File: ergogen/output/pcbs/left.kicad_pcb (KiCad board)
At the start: 2 copper layers, 118.4 x 104.8 mm, 29 parts

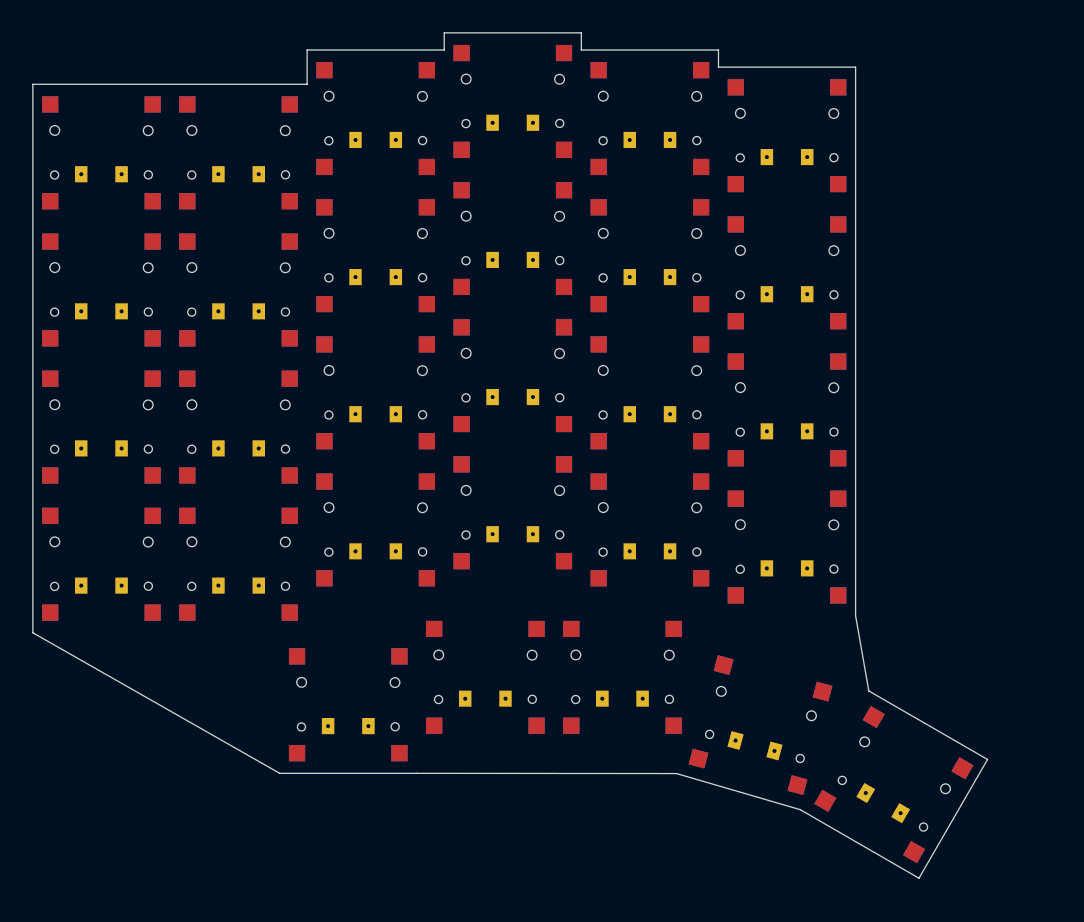
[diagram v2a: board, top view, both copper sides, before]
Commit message: feat: improved outlines
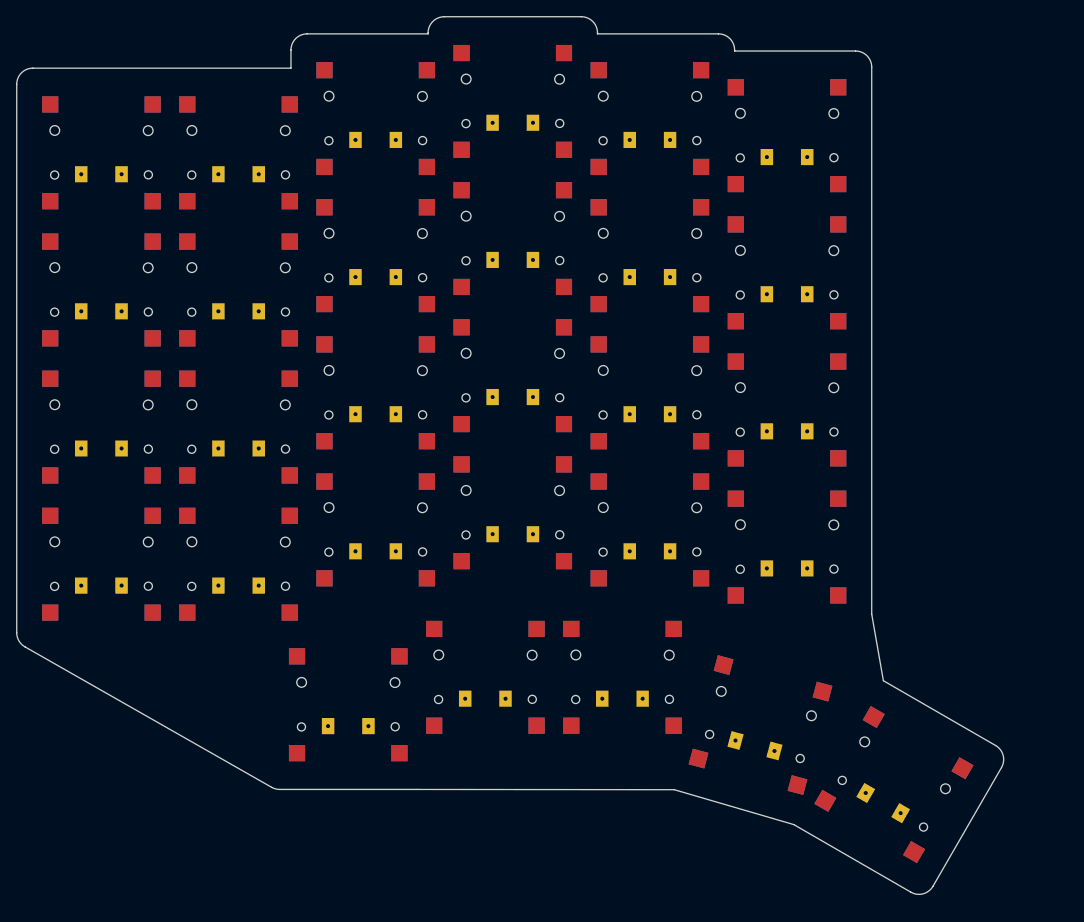
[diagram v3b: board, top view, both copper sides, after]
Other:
- board size 118.4 x 104.8 mm -> 122.4 x 108.8 mm
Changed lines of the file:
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@@
 (model "models/PG1316S--装配体.STEP" (offset (xyz -4.75 -6.25 -10.25)) (scale (xyz 1 1 1)) (rotate (xyz 0 0 0)))
 )
-  (gr_line (start 91.5 108.5) (end 91.5 40.5) (layer Edge.Cuts) (stroke (width 0.15) (type default)))
-(gr_line (start 91.5 40.5) (end 125.5 40.5) (layer Edge.Cuts) (stroke (width 0.15) (type default)))
-(gr_line (start 125.5 40.5) (end 125.5 36.25) (layer Edge.Cuts) (stroke (width 0.15) (type default)))
-(gr_line (start 125.5 36.25) (end 142.5 36.25) (layer Edge.Cuts) (stroke (width 0.15) (type default)))
-(gr_line (start 142.5 36.25) (end 142.5 34.125) (layer Edge.Cuts) (stroke (width 0.15) (type default)))
-(gr_line (start 142.5 34.125) (end 159.5 34.125) (layer Edge.Cuts) (stroke (width 0.15) (type default)))
-(gr_line (start 159.5 34.125) (end 159.5 36.25) (layer Edge.Cuts) (stroke (width 0.15) (type default)))
-(gr_line (start 159.5 36.25) (end 176.5 36.25) (layer Edge.Cuts) (stroke (width 0.15) (type default)))
-(gr_line (start 176.5 36.25) (end 176.5 38.375) (layer Edge.Cuts) (stroke (width 0.15) (type default)))
-(gr_line (start 176.5 38.375) (end 193.5 38.375) (layer Edge.Cuts) (stroke (width 0.15) (type default)))
-(gr_line (start 193.5 38.375) (end 193.5 106.375) (layer Edge.Cuts) (stroke (width 0.15) (type default)))
-(gr_line (start 193.5 106.375) (end 195.1372799 115.70819429999999) (layer Edge.Cuts) (stroke (width 0.15) (type default)))
-(gr_line (start 195.1372799 115.70819429999999) (end 209.8597117 124.20819429999999) (layer Edge.Cuts) (stroke (width 0.15) (type default)))
-(gr_line (start 209.8597117 124.20819429999999) (end 201.3597117 138.93062609999998) (layer Edge.Cuts) (stroke (width 0.15) (type default)))
-(gr_line (start 201.3597117 138.93062609999998) (end 186.6372799 130.43062609999998) (layer Edge.Cuts) (stroke (width 0.15) (type default)))
-(gr_line (start 186.6372799 130.43062609999998) (end 171.3055208 125.9554228) (layer Edge.Cuts) (stroke (width 0.15) (type default)))
-(gr_line (start 171.3055208 125.9554228) (end 139.1 125.925) (layer Edge.Cuts) (stroke (width 0.15) (type default)))
-(gr_line (start 139.1 125.925) (end 122.1 125.925) (layer Edge.Cuts) (stroke (width 0.15) (type default)))
-(gr_line (start 122.1 125.925) (end 91.5 108.5) (layer Edge.Cuts) (stroke (width 0.15) (type default)))
+  (gr_line (start 89.5 108.5) (end 89.5 40.5) (layer Edge.Cuts) (stroke (width 0.15) (type default)))
+(gr_arc (start 91.5 38.5) (mid 90.0857864 39.0857864) (end 89.5 40.5) (layer Edge.Cuts) (stroke (width 0.15) (type default)))
+(gr_line (start 91.5 38.5) (end 123.5 38.5) (layer Edge.Cuts) (stroke (width 0.15) (type default)))
+(gr_line (start 123.5 38.5) (end 123.5 36.25) (layer Edge.Cuts) (stroke (width 0.15) (type default)))
+(gr_arc (start 125.5 34.25) (mid 124.0857864 34.8357864) (end 123.5 36.25) (layer Edge.Cuts) (stroke (width 0.15) (type default)))
+(gr_line (start 125.5 34.25) (end 140.5 34.25) (layer Edge.Cuts) (stroke (width 0.15) (type default)))
+(gr_line (start 140.5 34.25) (end 140.5 34.125) (layer Edge.Cuts) (stroke (width 0.15) (type default)))
+(gr_arc (start 142.5 32.125) (mid 141.0857864 32.7107864) (end 140.5 34.125) (layer Edge.Cuts) (stroke (width 0.15) (type default)))
+(gr_line (start 142.5 32.125) (end 159.5 32.125) (layer Edge.Cuts) (stroke (width 0.15) (type default)))
+(gr_arc (start 161.5 34.125) (mid 160.9142136 32.7107864) (end 159.5 32.125) (layer Edge.Cuts) (stroke (width 0.15) (type default)))
+(gr_line (start 161.5 34.125) (end 161.5 34.25) (layer Edge.Cuts) (stroke (width 0.15) (type default)))
+(gr_line (start 161.5 34.25) (end 176.5 34.25) (layer Edge.Cuts) (stroke (width 0.15) (type default)))
+(gr_arc (start 178.5 36.25) (mid 177.9142136 34.8357864) (end 176.5 34.25) (layer Edge.Cuts) (stroke (width 0.15) (type default)))
+(gr_line (start 178.5 36.25) (end 178.5 36.375) (layer Edge.Cuts) (stroke (width 0.15) (type default)))
+(gr_line (start 178.5 36.375) (end 193.5 36.375) (layer Edge.Cuts) (stroke (width 0.15) (type default)))
+(gr_arc (start 195.5 38.375) (mid 194.9142136 36.9607864) (end 193.5 36.375) (layer Edge.Cuts) (stroke (width 0.15) (type default)))
+(gr_line (start 195.5 38.375) (end 195.5 106.20090349023451) (layer Edge.Cuts) (stroke (width 0.15) (type default)))
+(gr_line (start 195.5 106.20090349023451) (end 196.94587069424657 114.44298361476274) (layer Edge.Cuts) (stroke (width 0.15) (type default)))
+(gr_line (start 196.94587069424657 114.44298361476254) (end 210.85971170000002 122.47614349999999) (layer Edge.Cuts) (stroke (width 0.15) (type default)))
+(gr_arc (start 211.59176250000002 125.20819429999999) (mid 211.7915633 123.69055619999999) (end 210.85971170000002 122.47614349999999) (layer Edge.Cuts) (stroke (width 0.15) (type default)))
+(gr_line (start 211.5917625 125.20819429999999) (end 203.0917625 139.93062609999998) (layer Edge.Cuts) (stroke (width 0.15) (type default)))
+(gr_arc (start 200.3597117 140.66267689999998) (mid 201.8773498 140.86247769999997) (end 203.0917625 139.93062609999998) (layer Edge.Cuts) (stroke (width 0.15) (type default)))
+(gr_line (start 200.3597117 140.66267689999998) (end 185.84577629334714 132.28305234935004) (layer Edge.Cuts) (stroke (width 0.15) (type default)))
+(gr_line (start 185.84577629334714 132.28305234935004) (end 171.0186700831264 127.95515271248252) (layer Edge.Cuts) (stroke (width 0.15) (type default)))
+(gr_line (start 171.0186700831264 127.9551527124825) (end 139.1 127.925) (layer Edge.Cuts) (stroke (width 0.15) (type default)))
+(gr_line (start 139.0981107 127.9249991) (end 122.1 127.925) (layer Edge.Cuts) (stroke (width 0.15) (type default)))
+(gr_arc (start 121.11032279999999 127.6629698) (mid 121.58811109999999 127.858383) (end 122.1 127.925) (layer Edge.Cuts) (stroke (width 0.15) (type default)))
+(gr_line (start 121.11032279999999 127.6629698) (end 90.5103228 110.2379698) (layer Edge.Cuts) (stroke (width 0.15) (type default)))
+(gr_arc (start 89.5 108.5) (mid 89.7709317 109.5051481) (end 90.5103228 110.2379698) (layer Edge.Cuts) (stroke (width 0.15) (type default)))
 )

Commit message: feat: refining bottom row
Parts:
- removed S29: , CPG1316S01D02_reversible
- moved S28 24.9 mm to (206.1, 114.7)
- moved S25 20.5 mm to (151.0, 115.7)
- moved S26 20.5 mm to (168.0, 115.7)
- moved S27 20.5 mm to (185.0, 115.7)
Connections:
- S25 pad 1: C1 -> C2
- S26 pad 1: C2 -> C3
- S26 pad 2: mid_home -> outward_home
- S27 pad 1: C3 -> C4
- S27 pad 2: outward_home -> small_thumbkey_home
- S28 pad 1: C4 -> C5
- S28 pad 2: small_thumbkey_home -> thumbkey_home
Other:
- board size 122.4 x 108.8 mm -> 129 x 95 mm

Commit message: feat: thumb key 1.5u (thanks @chadtrans)
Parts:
- turned S28 to 75 degrees
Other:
- board size 129 x 95 mm -> 130 x 99.4 mm
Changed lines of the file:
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@@
 )
 (footprint "CPG1316S01D02_reversible"
-(at 206.1051848 114.6999809 -15)
+(at 206.1051848 114.6999809 75)
 (layer F.Cu)
 (attr smd)
-(property "Reference" "S28" hide (at 0 0 -15) (layer "F.SilkS") (effects (font (size 1 1) (thickness 0.15))))
-(pad "1" thru_hole rect (at -2.5 2.65 -15) (size 1.55 2) (drill 0.5) (layers "*.Cu" "*.Mask") (remove_unused_layers no) (thermal_bridge_angle 45) (net 26 "C5"))
-(pad "2" thru_hole rect (at 2.5 2.65 -15) (size 1.55 2) (drill 0.5) (layers "*.Cu" "*.Mask") (remove_unused_layers no) (thermal_bridge_angle 45) (net 34 "thumbkey_home"))
-(pad "3" smd rect (at -6.35 -6 -15) (size 2 2) (layers "F.Cu" "F.Paste" "F.Mask") (thermal_bridge_angle 45) (net 0 ""))
-(pad "3" smd rect (at -6.35 -6 -15) (size 2 2) (layers "B.Cu" "B.Paste" "B.Mask") (thermal_bridge_angle 45) (net 0 ""))
-(pad "3" smd rect (at -6.35 6 -15) (size 2 2) (layers "F.Cu" "F.Paste" "F.Mask") (thermal_bridge_angle 45) (net 0 ""))
-(pad "3" smd rect (at -6.35 6 -15) (size 2 2) (layers "B.Cu" "B.Paste" "B.Mask") (thermal_bridge_angle 45) (net 0 ""))
-(pad "3" smd rect (at 6.35 -6 -15) (size 2 2) (layers "F.Cu" "F.Paste" "F.Mask") (thermal_bridge_angle 45) (net 0 ""))
-(pad "3" smd rect (at 6.35 -6 -15) (size 2 2) (layers "B.Cu" "B.Paste" "B.Mask") (thermal_bridge_angle 45) (net 0 ""))
-(pad "3" smd rect (at 6.35 6 -15) (size 2 2) (layers "F.Cu" "F.Paste" "F.Mask") (thermal_bridge_angle 45) (net 0 ""))
-(pad "3" smd rect (at 6.35 6 -15) (size 2 2) (layers "B.Cu" "B.Paste" "B.Mask") (thermal_bridge_angle 45) (net 0 ""))
+(property "Reference" "S28" hide (at 0 0 75) (layer "F.SilkS") (effects (font (size 1 1) (thickness 0.15))))
+(pad "1" thru_hole rect (at -2.5 2.65 75) (size 1.55 2) (drill 0.5) (layers "*.Cu" "*.Mask") (remove_unused_layers no) (thermal_bridge_angle 45) (net 26 "C5"))
+(pad "2" thru_hole rect (at 2.5 2.65 75) (size 1.55 2) (drill 0.5) (layers "*.Cu" "*.Mask") (remove_unused_layers no) (thermal_bridge_angle 45) (net 34 "thumbkey_home"))
+(pad "3" smd rect (at -6.35 -6 75) (size 2 2) (layers "F.Cu" "F.Paste" "F.Mask") (thermal_bridge_angle 45) (net 0 ""))
+(pad "3" smd rect (at -6.35 -6 75) (size 2 2) (layers "B.Cu" "B.Paste" "B.Mask") (thermal_bridge_angle 45) (net 0 ""))
+(pad "3" smd rect (at -6.35 6 75) (size 2 2) (layers "F.Cu" "F.Paste" "F.Mask") (thermal_bridge_angle 45) (net 0 ""))
+(pad "3" smd rect (at -6.35 6 75) (size 2 2) (layers "B.Cu" "B.Paste" "B.Mask") (thermal_bridge_angle 45) (net 0 ""))
+(pad "3" smd rect (at 6.35 -6 75) (size 2 2) (layers "F.Cu" "F.Paste" "F.Mask") (thermal_bridge_angle 45) (net 0 ""))
+(pad "3" smd rect (at 6.35 -6 75) (size 2 2) (layers "B.Cu" "B.Paste" "B.Mask") (thermal_bridge_angle 45) (net 0 ""))
+(pad "3" smd rect (at 6.35 6 75) (size 2 2) (layers "F.Cu" "F.Paste" "F.Mask") (thermal_bridge_angle 45) (net 0 ""))
+(pad "3" smd rect (at 6.35 6 75) (size 2 2) (layers "B.Cu" "B.Paste" "B.Mask") (thermal_bridge_angle 45) (net 0 ""))
 (fp_circle (center -5.8 2.75) (end -5.3 2.75) (stroke (width 0.1) (type default)) (fill none) (layer "Edge.Cuts"))
 (fp_circle (center -5.781 -2.773) (end -6.381 -2.773) (stroke (width 0.1) (type default)) (fill none) (layer "Edge.Cuts"))
@@
 (gr_line (start 178.5 36.375) (end 193.5 36.375) (layer Edge.Cuts) (stroke (width 0.15) (type default)))
 (gr_arc (start 195.5 38.375) (mid 194.9142136 36.9607864) (end 193.5 36.375) (layer Edge.Cuts) (stroke (width 0.15) (type default)))
-(gr_line (start 195.5 38.375) (end 195.5 103.64496668730112) (layer Edge.Cuts) (stroke (width 0.15) (type default)))
-(gr_line (start 195.5 103.64496668730112) (end 199.4917811 102.3827159) (layer Edge.Cuts) (stroke (width 0.15) (type default)))
-(gr_arc (start 200.6124153 102.3577978) (mid 200.05031680000002 102.2901437) (end 199.4917811 102.3827159) (layer Edge.Cuts) (stroke (width 0.15) (type default)))
-(gr_line (start 200.61241529999998 102.3577978) (end 217.03315429999998 106.7577216) (layer Edge.Cuts) (stroke (width 0.15) (type default)))
-(gr_arc (start 218.4473679 109.20721139999999) (mid 218.24756709999997 107.68957329999999) (end 217.03315429999998 106.7577216) (layer Edge.Cuts) (stroke (width 0.15) (type default)))
-(gr_line (start 218.4473679 109.2072114) (end 214.04744409999998 125.6279504) (layer Edge.Cuts) (stroke (width 0.15) (type default)))
-(gr_arc (start 211.59795429999997 127.042164) (mid 213.11559239999997 126.84236320000001) (end 214.04744409999998 125.6279504) (layer Edge.Cuts) (stroke (width 0.15) (type default)))
-(gr_line (start 211.5979543 127.042164) (end 195.61215207761586 122.7587811595346) (layer Edge.Cuts) (stroke (width 0.15) (type default)))
-(gr_line (start 195.61215207761586 122.7587811595346) (end 176.860215 126.1922939) (layer Edge.Cuts) (stroke (width 0.15) (type default)))
-(gr_arc (start 176.5 126.225) (mid 176.6808484 126.21680669999999) (end 176.860215 126.1922939) (layer Edge.Cuts) (stroke (width 0.15) (type default)))
-(gr_line (start 142.5 126.225) (end 176.5 126.225) (layer Edge.Cuts) (stroke (width 0.15) (type default)))
+(gr_line (start 195.5 114.6761103767177) (end 195.5 38.375) (layer Edge.Cuts) (stroke (width 0.15) (type default)))
+(gr_line (start 142.5 126.225) (end 192.99725940000002 126.225) (layer Edge.Cuts) (stroke (width 0.15) (type default)))
 (gr_arc (start 141.9107092 126.1362133) (mid 142.2020291 126.2026788) (end 142.5 126.225) (layer Edge.Cuts) (stroke (width 0.15) (type default)))
 (gr_line (start 141.9107092 126.1362133) (end 90.9107092 110.4112133) (layer Edge.Cuts) (stroke (width 0.15) (type default)))
 (gr_arc (start 89.5 108.5) (mid 89.8908727 109.6877328) (end 90.9107092 110.4112133) (layer Edge.Cuts) (stroke (width 0.15) (type default)))
+(gr_line (start 212.6089246 130.0306526) (end 219.40292449999998 104.6750997) (layer Edge.Cuts) (stroke (width 0.15) (type default)))
+(gr_arc (start 219.40292449999998 104.6750997) (mid 219.20312359999997 103.1574616) (end 217.98871089999997 102.22560990000001) (layer Edge.Cuts) (stroke (width 0.15) (type default)))
+(gr_line (start 217.9887109 102.22560990000001) (end 202.0509348 97.9550956) (layer Edge.Cuts) (stroke (width 0.15) (type default)))
+(gr_arc (start 202.0509348 97.9550956) (mid 200.5332967 98.1548965) (end 199.60144499999998 99.3693092) (layer Edge.Cuts) (stroke (width 0.15) (type default)))
+(gr_line (start 199.60144499999998 99.3693092) (end 195.5 114.6761103767177) (layer Edge.Cuts) (stroke (width 0.15) (type default)))
+(gr_arc (start 192.99725940000002 126.225) (mid 193.5137967 126.8230538) (end 194.2216587 127.17435189999999) (layer Edge.Cuts) (stroke (width 0.15) (type default)))
+(gr_line (start 194.22165869999998 127.17435189999999) (end 210.15943479999999 131.4448662) (layer Edge.Cuts) (stroke (width 0.15) (type default)))
+(gr_arc (start 210.15943479999999 131.4448662) (mid 211.67707289999998 131.2450653) (end 212.6089246 130.0306526) (layer Edge.Cuts) (stroke (width 0.15) (type default)))
 )
